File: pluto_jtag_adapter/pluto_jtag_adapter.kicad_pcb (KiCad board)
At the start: 2 copper layers, 53 x 34.2 mm, 61 parts, among them J1 JTAG_UART_PLUTO, J2 Conn_01x08, J3 Conn_01x04, J4 USB_B_Micro, U1 FT2232HL, U2 AP2112K-3.3, U3 AP2112K-1.8, U4 93LC46B, U6 TXB0104D, U7 TLV7031DBV, U8 WE-TVS-82400102, U9 TXB0102DCU, Y1 7M-12.000MAAJ-T

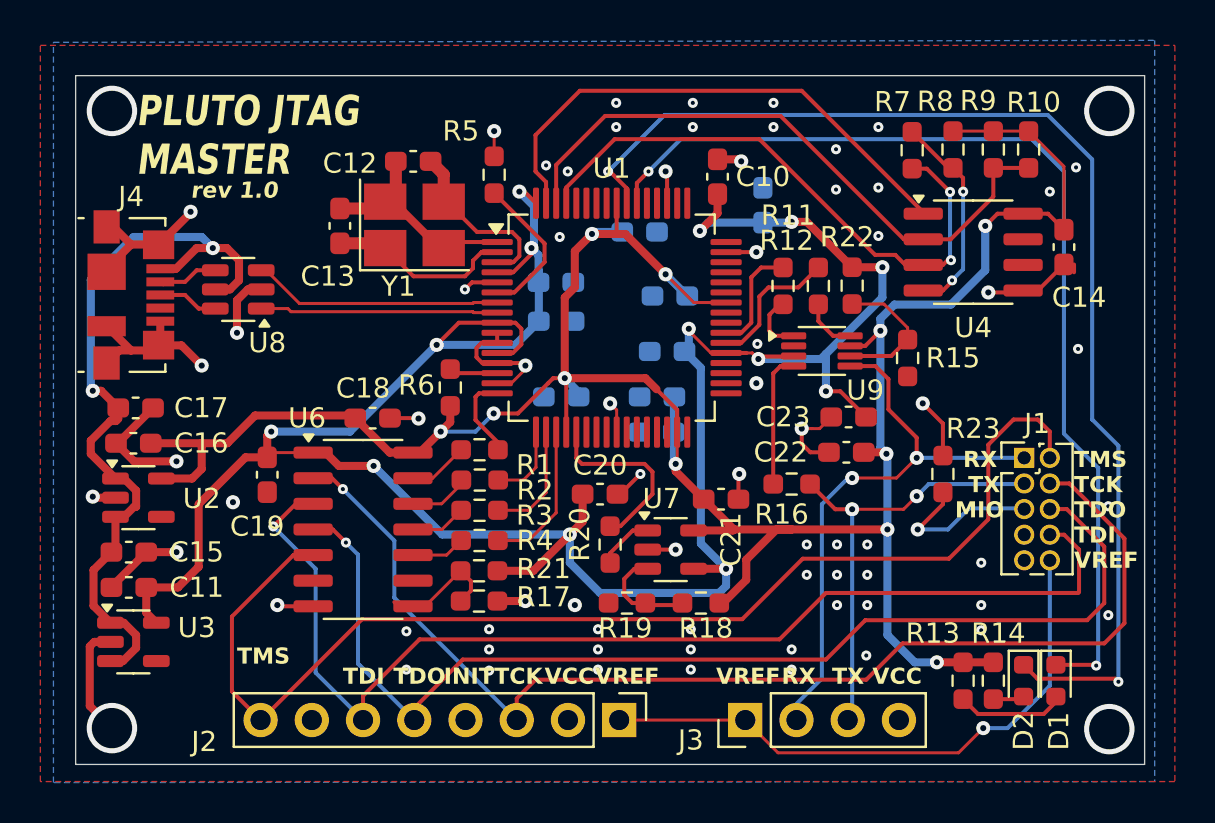
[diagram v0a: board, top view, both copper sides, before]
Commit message: Add correct supplies for VPHY and VPLL
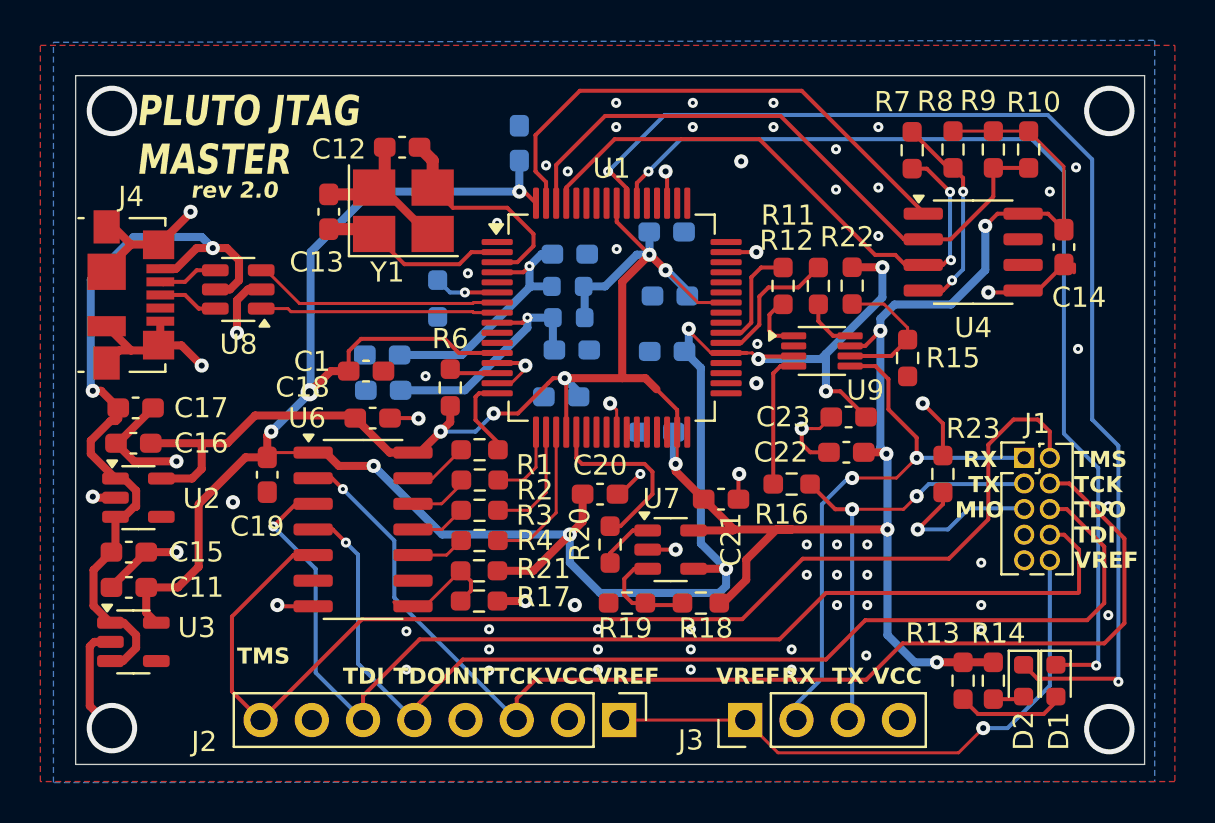
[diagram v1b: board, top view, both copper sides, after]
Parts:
- added C24: 100n, Capacitor_SMD:C_0603_1608Metric_Pad1.08x0.95mm_HandSolder, B.Cu at (118.6, 92.8)
- added FB1: BLM18BA121SH1D, Inductor_SMD:L_0603_1608Metric, B.Cu at (118.5, 91.2)
- added FB2: BLM18BA121SH1D, Inductor_SMD:L_0603_1608Metric, B.Cu at (118.4, 89.7)
- C1: moved to F.Cu
- C10: value 4u7 -> 100n; moved to B.Cu
- R5: moved to B.Cu
- moved C9 20.3 mm to (109.2, 93.1), turned to 180 degrees
- moved C8 13.6 mm to (109.2, 94.8)
- moved C1 10.4 mm to (108.4, 93.9)
- moved C2 9.01 mm to (116.0, 82.6), turned to 90 degrees
- moved C10 8.27 mm to (118.5, 88.1), turned to 0 degrees
- moved R5 6.75 mm to (112.0, 90.3), turned to -90 degrees
- moved C4 1.34 mm to (123.3, 87.0)
- moved C12 0.89 mm to (110.2, 82.8)
- moved C13 0.89 mm to (106.5, 86.0)
- moved Y1 0.89 mm to (110.2, 86.0)
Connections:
- C10 pad 1: +1V8 -> Net-(U1-VPHY)
- C8 pad 1: +3.3V -> Net-(U1-VPLL)
- C9 pad 1: +1V8 -> Net-(U1-VPHY)
- U1 pad 4: +1V8 -> Net-(U1-VPHY)
- U1 pad 9: +1V8 -> Net-(U1-VPLL)
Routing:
- net Net-(U1-VPHY): track 0.00 -> 13.2 mm, vias 0 -> 1
- net Net-(U1-VPLL): track 0.00 -> 12.6 mm, vias 0 -> 1
- net GND: track 82.8 -> 70.9 mm, vias 74 -> 75
- net +1V8: track 127.5 -> 117.8 mm, vias 13 -> 10
- net Net-(U1-REF): track 7.43 -> 3.27 mm, vias 0 -> 1
- net Net-(U1-OSCO): track 8.85 -> 11.0 mm
- net +3.3V: track 132.0 -> 132.9 mm
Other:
- board text added: "rev 2.0"
- board text removed: "rev 1.0"
